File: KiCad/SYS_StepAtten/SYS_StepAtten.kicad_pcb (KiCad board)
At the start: 2 copper layers, 122 x 84 mm, 145 parts, among them J1 RCA-Out, J10 A/D GND Jumper, J11 ADJ_L, J12 ADJ_R, J2 RCA-1, J3 RCA-2, J4 AUX-1-2, J5 Barrel_Jack 9Vdc, J6 POT_EXT Conn, J7 cfg jumper, J8 ARM SWD, J9 A/D GND Jumper, K1 TQ2SA, K10 TQ2SA, K11 TQ2SA, K12 TQ2SA, K13 TQ2SA, K14 TQ2SA, K2 TQ2SA, K3 TQ2SA, K4 TQ2SA, K5 TQ2SA, K6 TQ2SA, K7 TQ2SA, K8 TQ2SA, K9 TQ2SA, Q1 2N7002, Q10 2N7002, Q11 2N7002, Q12 2N7002, Q13 2N7002, Q14 2N7002, Q2 2N7002, Q3 2N7002, Q4 2N7002, Q5 2N7002, Q6 2N7002, Q7 2N7002, Q8 2N7002, Q9 2N7002, SW1 INPUT_SWITCH, SW2 ON/OFF, U1 LM317, U2 MC34063AD, U4 STM32f030K6T6

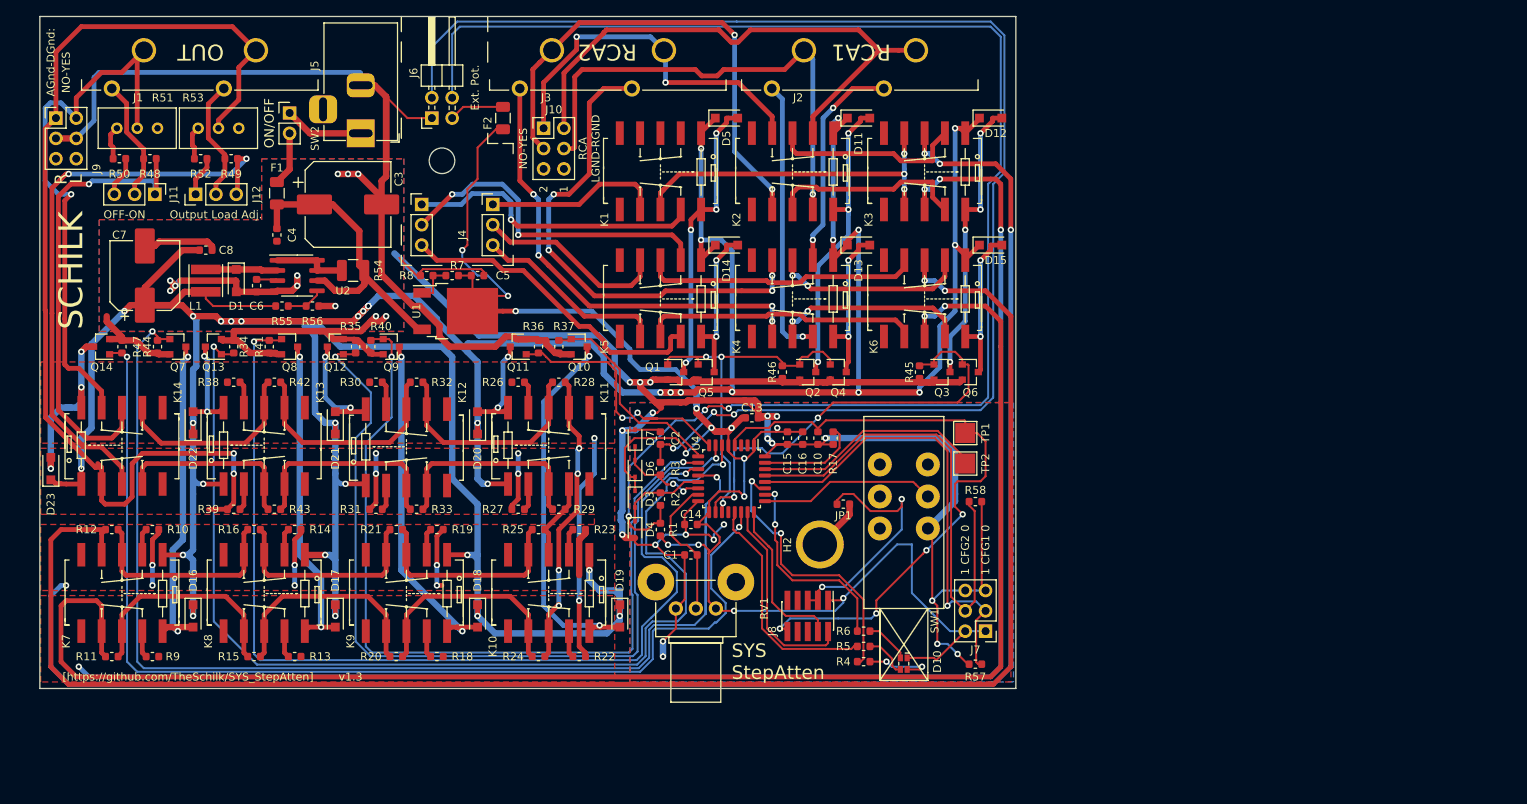
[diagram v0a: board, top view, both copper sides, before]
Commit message: Change relays and micro and USB c for power
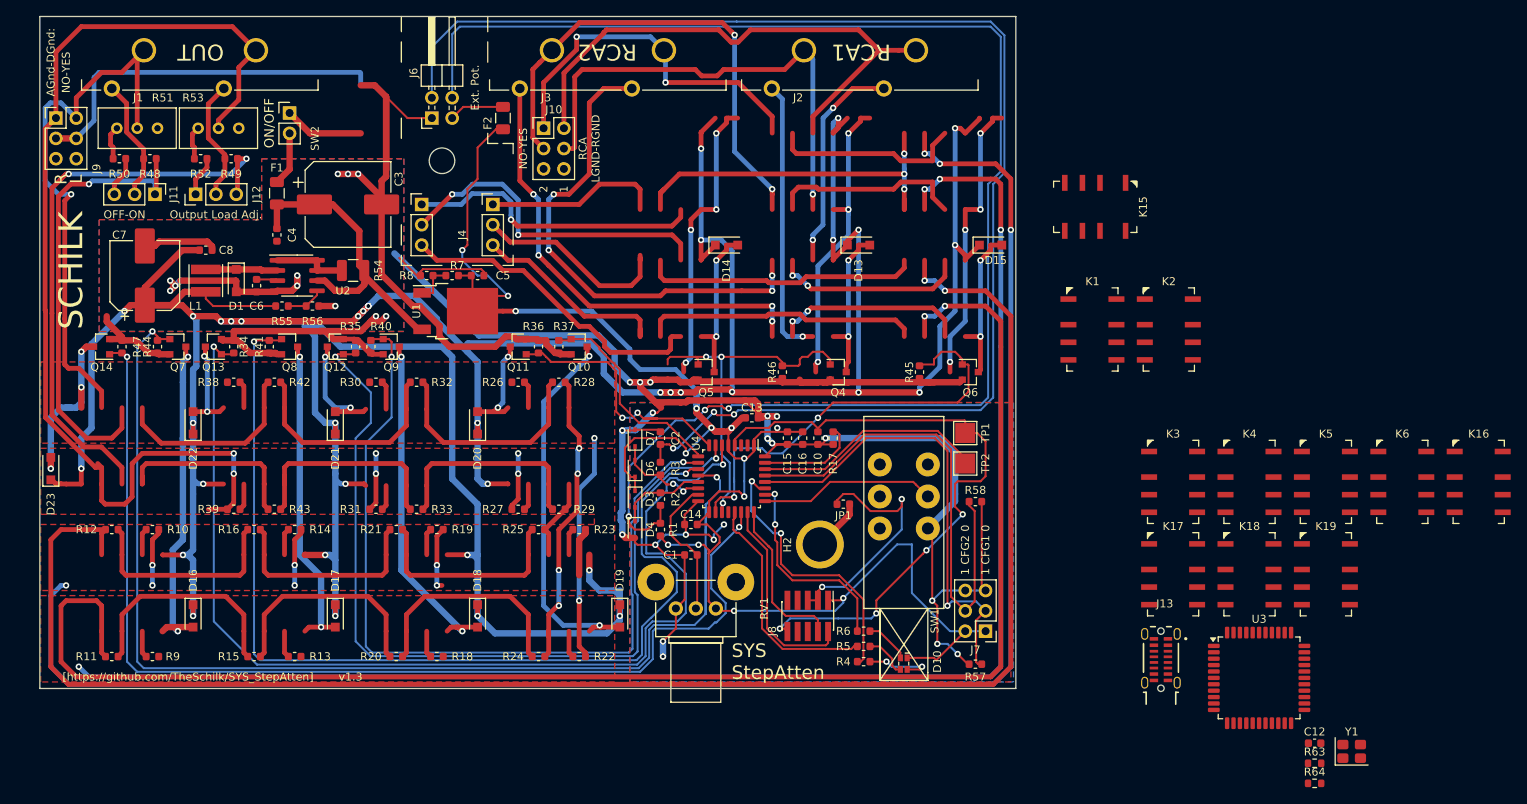
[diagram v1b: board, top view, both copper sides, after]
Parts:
- removed D11, D12, D5: 1N4001, Diode_SMD:D_SOD-123F
- removed G1: BarrelPolarity_CenterPos, BarrelPolarity_3mm:BarrelPolarity_3mm_CenterPos
- removed J5: Barrel_Jack 9Vdc, Connector_BarrelJack:BarrelJack_Horizontal
- removed K10, K11, K12, K13, K14, K7, K8, K9: TQ2SA, Panasonic_TQ2SA:Panasonic_TQ2SA
- removed Q1, Q2, Q3: 2N7002, Package_TO_SOT_SMD:SOT-23
- added C12: 1uf, Capacitor_SMD:C_0603_1608Metric, F.Cu at (237.3, 154.3)
- added J13: USB_C_Receptacle_USB2.0_16P, GCT_USB4210:GCT_USB4210-GF-A_REVA, F.Cu at (218.1, 149.5)
- added K15: IM03, Relay_SMD:Relay_2P2T_10x6mm_TE_IMxxG, F.Cu at (209.9, 87.3)
- added K16: IM03, Relay_SMD:Relay_2P2T_10x6mm_TE_IMxxG, F.Cu at (257.9, 121.7)
- added K17: IM03, Relay_SMD:Relay_2P2T_10x6mm_TE_IMxxG, F.Cu at (219.7, 133.2)
- added K18: IM03, Relay_SMD:Relay_2P2T_10x6mm_TE_IMxxG, F.Cu at (229.2, 133.2)
- added K19: IM03, Relay_SMD:Relay_2P2T_10x6mm_TE_IMxxG, F.Cu at (238.8, 133.2)
- added R63: 5K1, Resistor_SMD:R_0603_1608Metric, F.Cu at (237.3, 156.8)
- added R64: 5K1, Resistor_SMD:R_0603_1608Metric, F.Cu at (237.3, 159.4)
- added U3: ATmega32U4-A, Package_QFP:TQFP-44_10x10mm_P0.8mm, F.Cu at (230.4, 146.2)
- added Y1: ABM8-16.000MHZ-10-R60-B1U-T, Crystal:Crystal_SMD_Abracon_ABM8G-4Pin_3.2x2.5mm, F.Cu at (242.0, 155.4)
- K1, K2, K3, K4, K5, K6: value TQ2SA -> IM03; footprint Panasonic_TQ2SA:Panasonic_TQ2SA -> Relay_SMD:Relay_2P2T_10x6mm_TE_IMxxG
- moved K5 86.4 mm to (238.8, 121.7), turned to 0 degrees
- moved K6 64.1 mm to (248.3, 121.7), turned to 0 degrees
- moved K4 61.7 mm to (229.2, 121.7), turned to 0 degrees
- moved K1 57.6 mm to (209.6, 102.6), turned to 0 degrees
- moved K2 51.1 mm to (219.1, 102.6), turned to 0 degrees
- moved K3 50.0 mm to (219.7, 121.7), turned to 0 degrees
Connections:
- C3 pad 1: Net-(C3-Pad1) -> Net-(U2-Vin)
- C4 pad 1: Net-(C3-Pad1) -> Net-(U2-Vin)
- D13 pad 2: Net-(D13-Pad2) -> Net-(D13-A)
- D14 pad 2: Net-(D14-Pad2) -> Net-(D14-A)
- D15 pad 2: Net-(D15-Pad2) -> Net-(D15-A)
- D16 pad 2: Net-(D16-Pad2) -> Net-(D16-A)
- D17 pad 2: Net-(D17-Pad2) -> Net-(D17-A)
- D18 pad 2: Net-(D18-Pad2) -> Net-(D18-A)
- D19 pad 2: Net-(D19-Pad2) -> Net-(D19-A)
- F1 pad 1: Net-(C3-Pad1) -> +5V
- J1 pad 1: /AGND_L -> GNDA
- J1 pad 3: /AGND_R -> GNDA
- J10 pad 5: (no net) -> unconnected-(J10-Pin_5-Pad5)
- J10 pad 6: (no net) -> unconnected-(J10-Pin_6-Pad6)
- J2 pad 1: /RCA1_GNDL -> GNDA
- J2 pad 3: /RCA1_GNDR -> GNDA
- J3 pad 1: /RCA2_GNDL -> GNDA
- J3 pad 3: /RCA2_GNDR -> GNDA
- J4 pad B_S: /AUX2_GND -> GNDA
- J4 pad T_S: /AUX1_GND -> GNDA
- J8 pad 6: (no net) -> unconnected-(J8-Pin_6-Pad6)
- J8 pad 7: (no net) -> unconnected-(J8-Pin_7-Pad7)
- J8 pad 8: (no net) -> unconnected-(J8-Pin_8-Pad8)
- J8 pad 9: (no net) -> unconnected-(J8-Pin_9-Pad9)
- J9 pad 5: (no net) -> unconnected-(J9-Pin_5-Pad5)
- J9 pad 6: (no net) -> unconnected-(J9-Pin_6-Pad6)
- K1 pad 2: (no net) -> /AUX1_R
- K1 pad 3: (no net) -> /AUX_R
- K1 pad 4: (no net) -> /AUX2_R
- K1 pad 5: (no net) -> /AUX2_L
- K1 pad 6: (no net) -> /AUX_L
- K1 pad 7: /AUX2_GND -> /AUX1_L
- K1 pad 8: Net-(K1-Pad8) -> Net-(D14-A)
- K2 pad 2: /RCA1_GNDR -> /RCA_R
- K2 pad 3: Net-(K2-Pad3) -> /R
- K2 pad 4: /RCA2_GNDR -> /AUX_R
- K2 pad 5: (no net) -> /AUX_L
- K2 pad 6: (no net) -> /L
- K2 pad 7: /RCA2_GNDL -> /RCA_L
- K2 pad 8: Net-(K2-Pad8) -> Net-(D15-A)
- K3 pad 2: Net-(K2-Pad3) -> Net-(K3-Pad2)
- K3 pad 3: /AGND_R -> Net-(K3-Pad3)
- K3 pad 4: Net-(K1-Pad8) -> /R
- K3 pad 5: (no net) -> /L
- K3 pad 6: (no net) -> Net-(K3-Pad6)
- K3 pad 7: Net-(K1-Pad8) -> Net-(K3-Pad7)
- K3 pad 8: /AGND_L -> Net-(D16-A)
- K4 pad 2: /RCA1_R -> Net-(K4-Pad2)
- K4 pad 4: /RCA2_R -> Net-(K3-Pad3)
- K4 pad 5: (no net) -> Net-(K3-Pad6)
- K4 pad 6: (no net) -> Net-(K4-Pad6)
- K4 pad 7: /RCA2_L -> Net-(K4-Pad7)
- K4 pad 8: Net-(K4-Pad8) -> Net-(D17-A)
- K5 pad 2: /AUX1_R -> Net-(K5-Pad2)
- K5 pad 4: /AUX2_R -> Net-(K4-Pad3)
- K5 pad 5: (no net) -> Net-(K4-Pad6)
- K5 pad 6: (no net) -> Net-(K5-Pad6)
- K5 pad 7: /AUX2_L -> Net-(K5-Pad7)
- K5 pad 8: Net-(K5-Pad8) -> Net-(D18-A)
- K6 pad 2: Net-(K4-Pad3) -> Net-(K6-Pad2)
- K6 pad 3: Net-(K6-Pad3) -> Net-(K16-Pad4)
- K6 pad 5: (no net) -> Net-(K5-Pad6)
- K6 pad 6: (no net) -> Net-(K16-Pad5)
- K6 pad 7: Net-(K5-Pad8) -> Net-(K6-Pad7)
- K6 pad 8: Net-(K6-Pad8) -> Net-(D19-A)
- Q10 pad 3: Net-(D19-Pad2) -> Net-(D19-A)
- Q4 pad 1: /rly_selectL_2 -> /rly_selectL_3
- Q4 pad 3: Net-(D13-Pad2) -> Net-(D13-A)
- Q5 pad 3: Net-(D14-Pad2) -> Net-(D14-A)
- Q6 pad 3: Net-(D15-Pad2) -> Net-(D15-A)
- Q7 pad 3: Net-(D16-Pad2) -> Net-(D16-A)
- Q8 pad 3: Net-(D17-Pad2) -> Net-(D17-A)
- Q9 pad 3: Net-(D18-Pad2) -> Net-(D18-A)
- R10 pad 1: /AGND_R -> GNDA
- R10 pad 2: Net-(K7-Pad2) -> Net-(K3-Pad2)
- R11 pad 1: Net-(K7-Pad8) -> Net-(K3-Pad6)
- R11 pad 2: Net-(K6-Pad8) -> /L
- R12 pad 1: Net-(K7-Pad3) -> Net-(K3-Pad3)
- R12 pad 2: Net-(K6-Pad3) -> /R
- R13 pad 1: /AGND_L -> GNDA
- R13 pad 2: Net-(K8-Pad9) -> Net-(K4-Pad7)
- R14 pad 1: /AGND_R -> GNDA
- R14 pad 2: Net-(K8-Pad2) -> Net-(K4-Pad2)
- R15 pad 1: Net-(K8-Pad8) -> Net-(K4-Pad6)
- R15 pad 2: Net-(K7-Pad8) -> Net-(K3-Pad6)
- R16 pad 1: Net-(K8-Pad3) -> Net-(K4-Pad3)
- R16 pad 2: Net-(K7-Pad3) -> Net-(K3-Pad3)
- R18 pad 1: /AGND_L -> GNDA
- R18 pad 2: Net-(K9-Pad9) -> Net-(K5-Pad7)
- R19 pad 1: /AGND_R -> GNDA
- R19 pad 2: Net-(K9-Pad2) -> Net-(K5-Pad2)
- R20 pad 1: Net-(K10-Pad7) -> Net-(K5-Pad6)
- R20 pad 2: Net-(K8-Pad8) -> Net-(K4-Pad6)
- R21 pad 1: Net-(K10-Pad4) -> Net-(K5-Pad3)
- R21 pad 2: Net-(K8-Pad3) -> Net-(K4-Pad3)
- R22 pad 1: /AGND_L -> GNDA
- R22 pad 2: Net-(K10-Pad9) -> Net-(K6-Pad7)
- R23 pad 1: /AGND_R -> GNDA
- R23 pad 2: Net-(K10-Pad2) -> Net-(K6-Pad2)
- R24 pad 1: Net-(K10-Pad8) -> Net-(K16-Pad5)
- R24 pad 2: Net-(K10-Pad7) -> Net-(K5-Pad6)
- R25 pad 1: Net-(K10-Pad3) -> Net-(K16-Pad4)
- R25 pad 2: Net-(K10-Pad4) -> Net-(K5-Pad3)
- R26 pad 1: /AGND_L -> GNDA
- R27 pad 1: /AGND_R -> GNDA
- R28 pad 2: Net-(K10-Pad8) -> Net-(K16-Pad5)
- R29 pad 2: Net-(K10-Pad3) -> Net-(K16-Pad4)
- R30 pad 1: /AGND_L -> GNDA
- R31 pad 1: /AGND_R -> GNDA
- R38 pad 1: /AGND_L -> GNDA
- R39 pad 1: /AGND_R -> GNDA
- R51 pad 2: /AGND_L -> GNDA
- R53 pad 2: /AGND_R -> GNDA
- R54 pad 2: Net-(C3-Pad1) -> Net-(U2-Vin)
- R9 pad 1: /AGND_L -> GNDA
- R9 pad 2: Net-(K7-Pad9) -> Net-(K3-Pad7)
- SW1 pad 1: (no net) -> unconnected-(SW1A-A-Pad1)
- SW1 pad 2: (no net) -> unconnected-(SW1A-B-Pad2)
- SW1 pad 3: (no net) -> unconnected-(SW1A-C-Pad3)
- U1 pad 3: Net-(C3-Pad1) -> unconnected-(U1-VI-Pad3)
- U2 pad 6: Net-(C3-Pad1) -> Net-(U2-Vin)
- U4 pad 1: +3V3 -> unconnected-(U4-VDD-Pad1)
- U4 pad 10: /rly_atten4 -> /rly_atten3
- U4 pad 11: /rly_atten5 -> /rly_atten4
- U4 pad 12: /rly_atten6 -> /rly_atten5
- U4 pad 13: /extctrl_sense -> /rly_atten6
- U4 pad 18: /rly_selectL_1 -> /extctrl_sense
- U4 pad 19: /rly_selectL_2 -> /rly_selectL_1
- U4 pad 2: (no net) -> unconnected-(U4-PF0-Pad2)
- U4 pad 20: (no net) -> /rly_selectL_2
- U4 pad 21: /led1 -> unconnected-(U4-PA11-Pad21)
- U4 pad 22: /rly_mute -> /led1
- U4 pad 23: /SWDIO -> /rly_mute
- U4 pad 24: /SWDCLK -> /SWDIO
- U4 pad 25: /btn -> /SWDCLK
- U4 pad 3: (no net) -> unconnected-(U4-PF1-Pad3)
- U4 pad 5: +3V3 -> unconnected-(U4-VDDA-Pad5)
- U4 pad 6: /rly_atten0 -> unconnected-(U4-PA0-Pad6)
- U4 pad 7: /rly_atten1 -> /rly_atten0
- U4 pad 8: /rly_atten2 -> /rly_atten1
- U4 pad 9: /rly_atten3 -> /rly_atten2
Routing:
- net (no net): track 0.00 -> 321.5 mm, vias 0 -> 18
- net Net-(K6-Pad3): track 207.4 -> 0.00 mm, vias 2 -> 0
- net /R: track 0.00 -> 207.4 mm, vias 0 -> 2
- net Net-(K6-Pad8): track 194.5 -> 0.00 mm, vias 2 -> 0
- net /L: track 0.00 -> 194.5 mm, vias 0 -> 2
- net GNDA: track 0.00 -> 131.3 mm, vias 0 -> 13
- net Net-(D16-Pad2): track 57.7 -> 0.00 mm, vias 2 -> 0
- net Net-(D16-A): track 0.00 -> 57.7 mm, vias 0 -> 2
- net Net-(D19-Pad2): track 47.2 -> 0.00 mm, vias 2 -> 0
- net Net-(D19-A): track 0.00 -> 47.2 mm, vias 0 -> 2
- net Net-(K1-Pad8): track 45.0 -> 0.00 mm, vias 3 -> 0
- net Net-(D18-A): track 0.00 -> 43.8 mm, vias 0 -> 2
- net Net-(D18-Pad2): track 43.8 -> 0.00 mm, vias 2 -> 0
- net /AGND_R: track 383.4 -> 340.2 mm, vias 16 -> 6
- net Net-(D17-Pad2): track 40.3 -> 0.00 mm, vias 2 -> 0
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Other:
- net class Default removed
